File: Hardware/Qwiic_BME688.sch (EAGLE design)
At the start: 30 parts, among them J2 QWIIC_RA, J4 QWIIC_RA, U1 BME688LGA

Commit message: Fixed formatting of examples
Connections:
- net SCL renamed SCL/SCK
- net SDA/POCI renamed SDA/PICO
- removed net SDO: ADR.2, J3.6
- removed net SDO/PICO: U1.SDO
- new net SDO/POCI: ADR.2, J3.6, U1.SDO
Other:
- note added: "NOTE: This circuitry defaults to I2C communication (address 0x76). If you wish to communicate over SPI, please cut the CSB jumper AND the ADR jumper. Remove the I2C pullup resistors by cutting the I2C jumper. Then use the SDO, SDI, SCK, and CSB holes on the board edge."
- note added: "v10"
- note removed: "NOTE: This circuitry defaults to I2C communication (address 0x76). If you wish to communicate over SPI, please cut the CSB jumper AND the ADR jumper. Then use the SDO, SDI, SCK, and CSB holes on the board edge."
- note removed: "v01"
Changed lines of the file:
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@@
 <sheet>
 <plain>
-<text x="237.744" y="7.366" size="2.54" layer="94" font="vector">v01</text>
+<text x="237.744" y="7.366" size="2.54" layer="94" font="vector">v10</text>
 <text x="210.82" y="111.76" size="1.778" layer="97" font="vector" align="center">Default, 7-bit unshifted
 I2C address: 0x76</text>
@@
 0x76). If you wish to communicate
 over SPI, please cut the CSB jumper
-AND the ADR jumper. Then use the
-SDO, SDI, SCK, and CSB holes on the
-board edge.</text>
+AND the ADR jumper. Remove the I2C
+pullup resistors by cutting the I2C
+jumper. Then use the SDO, SDI, SCK,
+and CSB holes on the board edge.</text>
 </plain>
 <instances>
@@
 </segment>
 </net>
-<net name="SCL" class="0">
+<net name="SCL/SCK" class="0">
 <segment>
 <pinref part="J2" gate="G$1" pin="4"/>
@@
 </segment>
 </net>
-<net name="SDA/POCI" class="0">
+<net name="SDA/PICO" class="0">
 <segment>
 <pinref part="J2" gate="G$1" pin="3"/>
@@
 <wire x1="190.5" y1="162.56" x2="193.04" y2="162.56" width="0.1524" layer="91"/>
 <wire x1="193.04" y1="162.56" x2="193.04" y2="160.02" width="0.1524" layer="91"/>
-</segment>
-</net>
-<net name="SDO" class="0">
-<segment>
-<pinref part="ADR" gate="G$1" pin="2"/>
-<wire x1="180.34" y1="93.98" x2="177.8" y2="93.98" width="0.1524" layer="91"/>
-<label x="177.8" y="93.98" size="1.27" layer="95" rot="R180" xref="yes"/>
-</segment>
-<segment>
-<pinref part="J3" gate="G$1" pin="6"/>
-<wire x1="78.74" y1="15.24" x2="73.66" y2="15.24" width="0.1524" layer="91"/>
-<label x="73.66" y="15.24" size="1.27" layer="95" rot="R180" xref="yes"/>
 </segment>
 </net>
@@
 </segment>
 </net>
-<net name="SDO/PICO" class="0">
+<net name="SDO/POCI" class="0">
 <segment>
 <pinref part="U1" gate="U1" pin="SDO"/>
@@
 <label x="142.24" y="93.98" size="1.27" layer="95" xref="yes"/>
 </segment>
-</net>
+<segment>
+<pinref part="ADR" gate="G$1" pin="2"/>
+<wire x1="180.34" y1="93.98" x2="177.8" y2="93.98" width="0.1524" layer="91"/>
+<label x="177.8" y="93.98" size="1.27" layer="95" rot="R180" xref="yes"/>
+</segment>
+<segment>
+<pinref part="J3" gate="G$1" pin="6"/>
+<wire x1="78.74" y1="15.24" x2="73.66" y2="15.24" width="0.1524" layer="91"/>
+<label x="73.66" y="15.24" size="1.27" layer="95" rot="R180" xref="yes"/>
+</segment>
+</net>

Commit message: Updates to hardware v02
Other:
- note added: "v02"
- note removed: "v10"
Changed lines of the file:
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@@
 <sheet>
 <plain>
-<text x="237.744" y="7.366" size="2.54" layer="94" font="vector">v10</text>
+<text x="237.744" y="7.366" size="2.54" layer="94" font="vector">v02</text>
 <text x="210.82" y="111.76" size="1.778" layer="97" font="vector" align="center">Default, 7-bit unshifted
 I2C address: 0x76</text>
@@
 <text x="58.42" y="165.1" size="1.778" layer="97" font="vector">Cut the LED jumper to
 disable the PWR LED</text>
-<text x="187.96" y="165.1" size="1.27" layer="97" font="vector">Cut I2C Jumper to remove
+<text x="187.96" y="165.1" size="1.778" layer="97" font="vector">Cut I2C Jumper to remove
 pullup resistors from the I2C bus</text>
 <text x="12.7" y="177.8" size="2.54" layer="94" font="vector" align="center">LED</text>

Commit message: Update version number
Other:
- note added: "v10"
- note removed: "v02"
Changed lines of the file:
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@@
 <sheet>
 <plain>
-<text x="237.744" y="7.366" size="2.54" layer="94" font="vector">v02</text>
+<text x="237.744" y="7.366" size="2.54" layer="94" font="vector">v10</text>
 <text x="210.82" y="111.76" size="1.778" layer="97" font="vector" align="center">Default, 7-bit unshifted
 I2C address: 0x76</text>

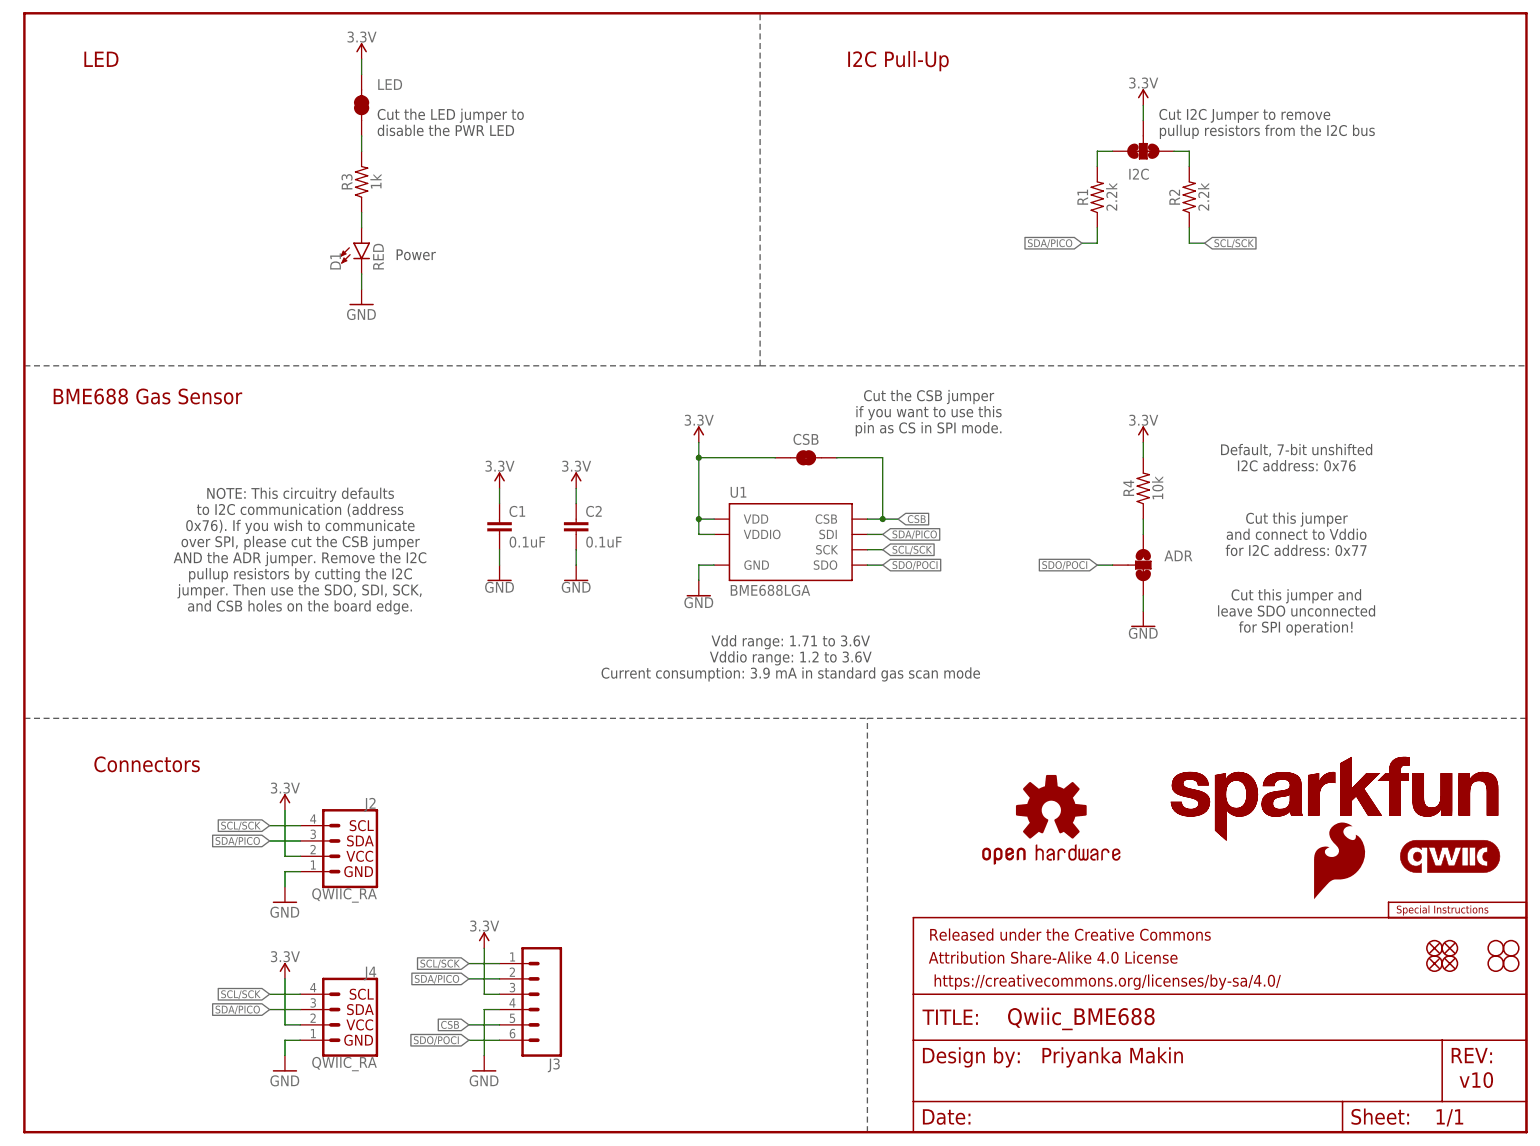
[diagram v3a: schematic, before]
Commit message: Design review changes
* Add table for jumper selection
* Nudge board name silk (on bottom) to avoid vias
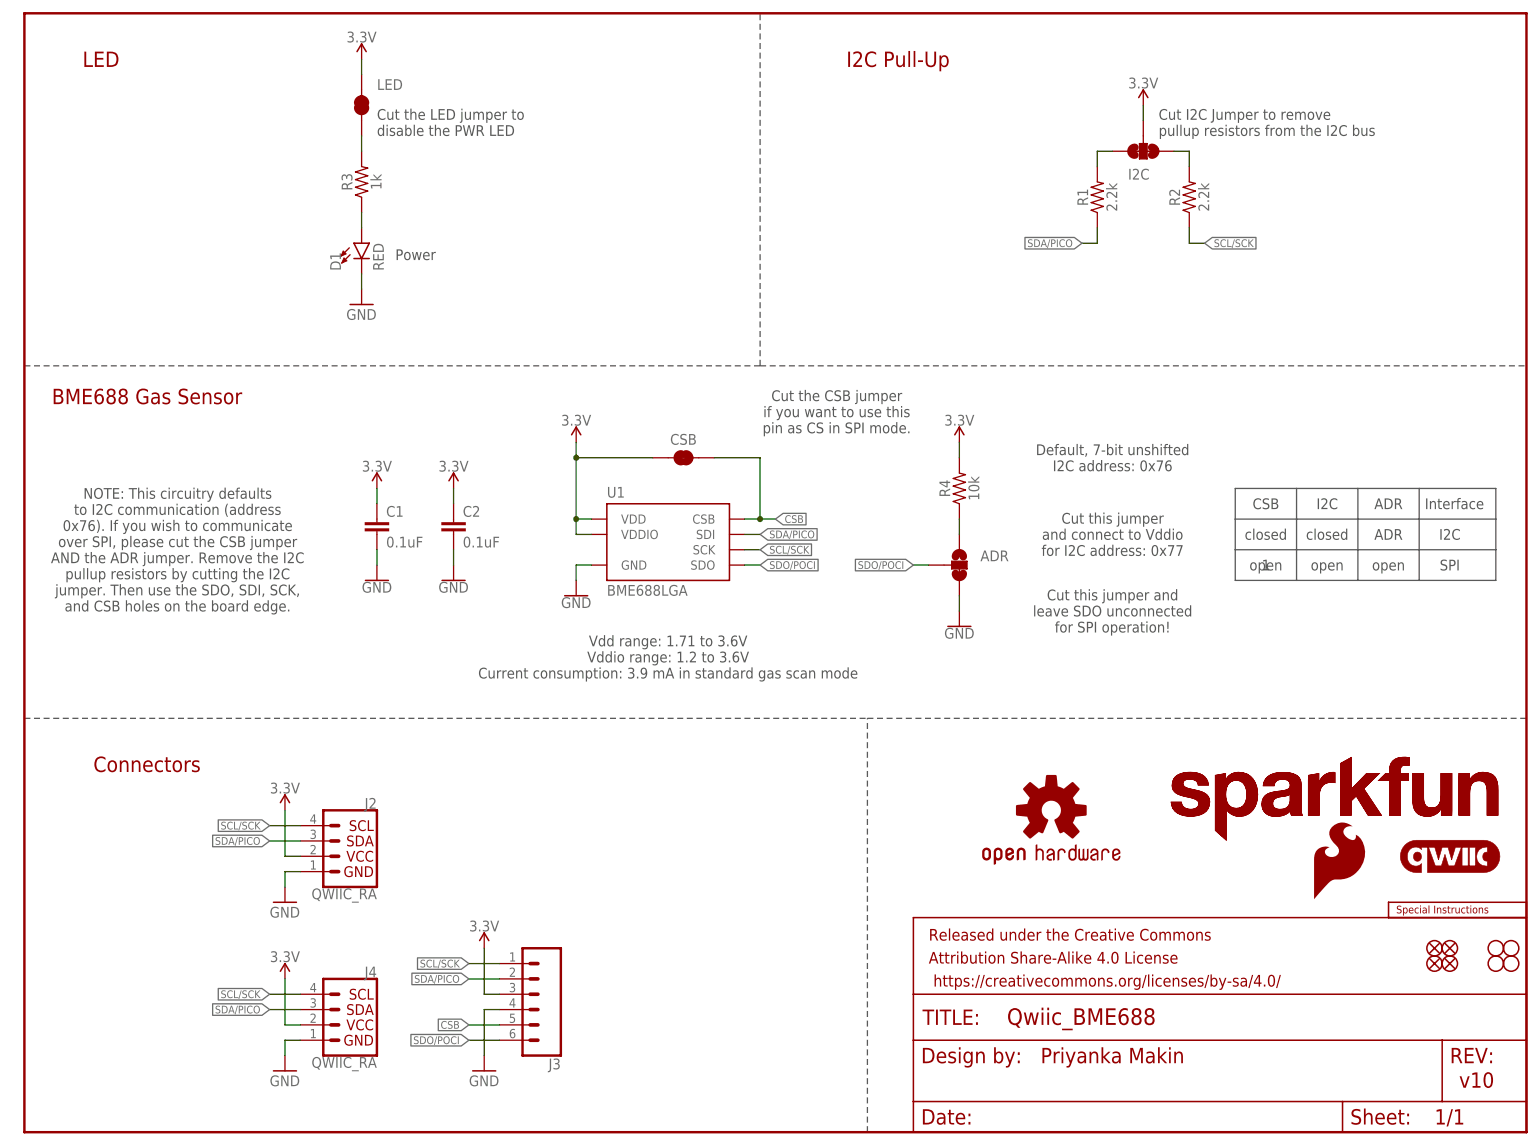
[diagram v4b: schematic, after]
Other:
- note added: "1"
- note added: "ADR"
- note added: "CSB"
- note added: "I2C"
- note added: "Interface"
- note added: "SPI"
- note added: "closed"
- note added: "open"
- moved on the sheet: ADR, C1, C2, CSB, R4, U1

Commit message: QC Double-check:
* Add active low line to "CSB" net label in the schematic
* Updated jumper selection table
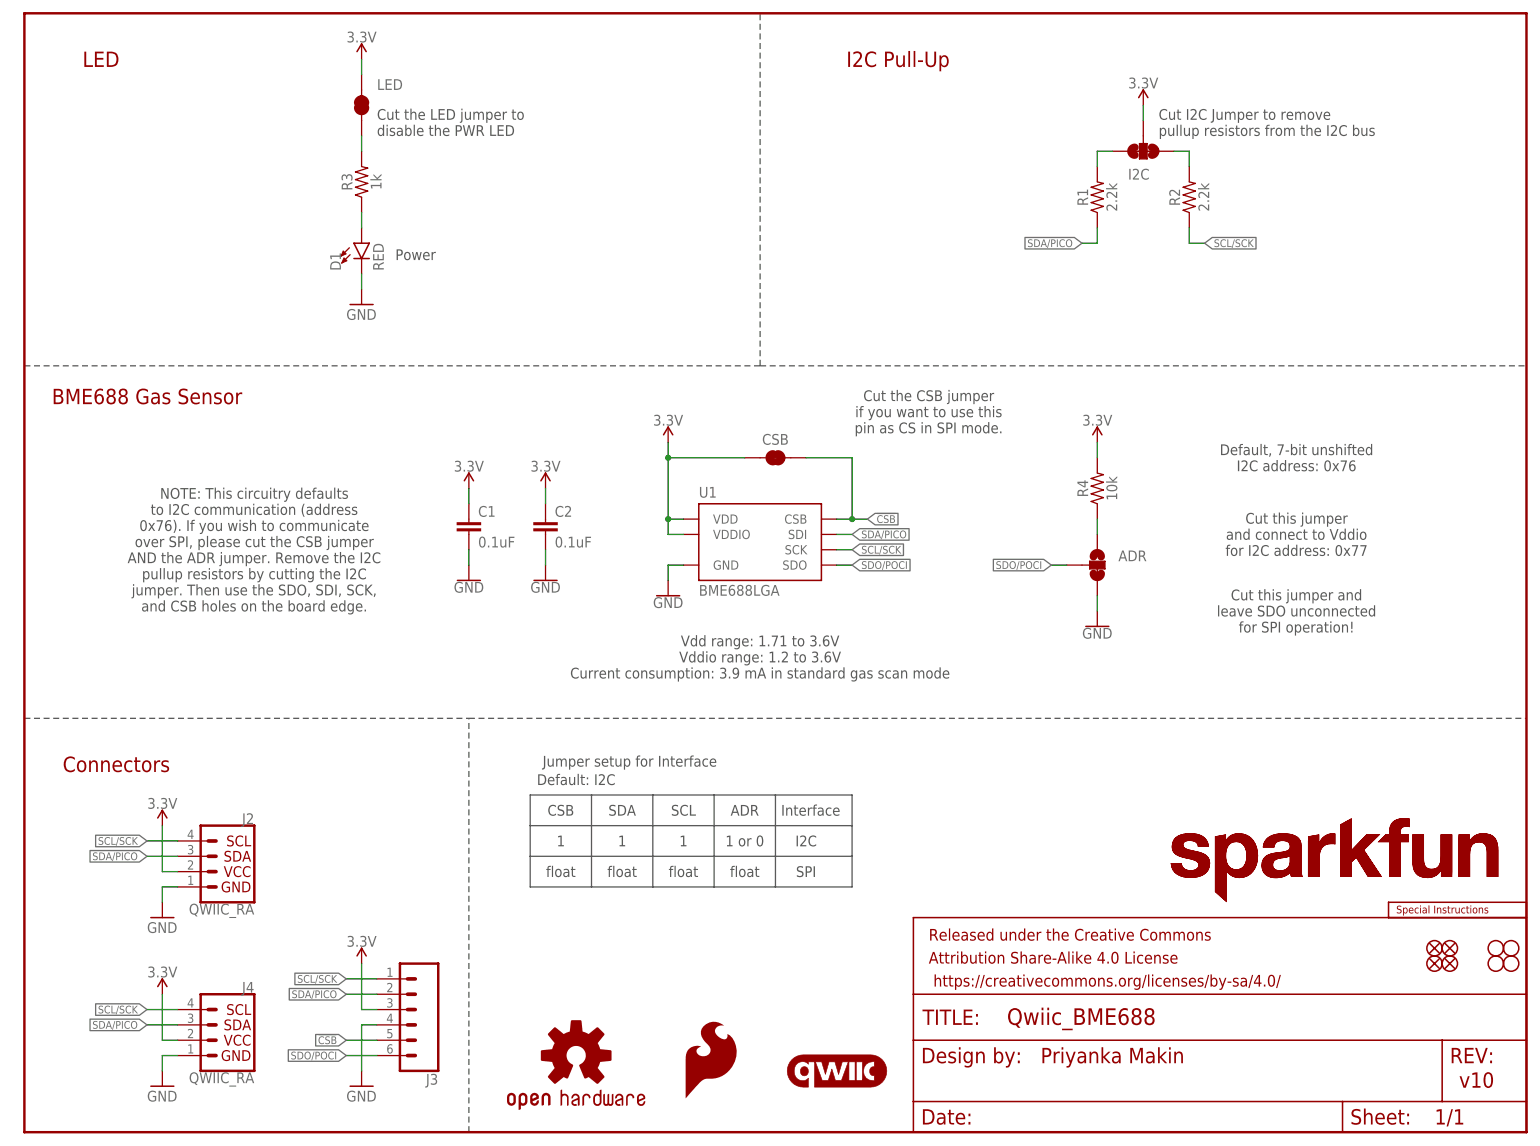
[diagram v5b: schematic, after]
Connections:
- net CSB renamed !CSB!
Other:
- note added: "1 or 0"
- note added: "Default: I2C"
- note added: "Jumper setup for Interface"
- note added: "SCL"
- note added: "SDA"
- note added: "float"
- note removed: "closed"
- note removed: "open"
- moved on the sheet: ADR, C1, C2, CSB, J2, J3, J4, R4, U1

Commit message: Update BME688 schematic symbol
* CSB pin to !CSB!
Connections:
- net !CSB!: now also U1.!CSB!; no longer U1.CSB
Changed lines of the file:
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@@
 <net name="!CSB!" class="0">
 <segment>
-<pinref part="U1" gate="U1" pin="CSB"/>
+<pinref part="U1" gate="U1" pin="!CSB!"/>
 <wire x1="134.62" y1="101.6" x2="137.16" y2="101.6" width="0.1524" layer="91"/>
 <label x="139.7" y="101.6" size="1.27" layer="95" xref="yes"/>
@@
 </sheet>
 </sheets>
-<errors>
-</errors>
 </schematic>
 </drawing>

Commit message: Rename PICO/POCI net labels to CIPO/COPI
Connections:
- net SDA/PICO renamed SDA/COPI
- net SDO/POCI renamed SDO/CIPO
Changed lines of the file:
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@@
 </segment>
 </net>
-<net name="SDA/PICO" class="0">
+<net name="SDA/COPI" class="0">
 <segment>
 <pinref part="J2" gate="G$1" pin="3"/>
@@
 </segment>
 </net>
-<net name="SDO/POCI" class="0">
+<net name="SDO/CIPO" class="0">
 <segment>
 <pinref part="U1" gate="U1" pin="SDO"/>

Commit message: Rename PICO/POCI labels to SDO/SDI
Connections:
- net SDA/COPI renamed SDI/SDA
- net SDO/CIPO renamed SDO
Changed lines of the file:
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@@
 </segment>
 </net>
-<net name="SDA/COPI" class="0">
+<net name="SDI/SDA" class="0">
 <segment>
 <pinref part="J2" gate="G$1" pin="3"/>
@@
 </segment>
 </net>
-<net name="SDO/CIPO" class="0">
+<net name="SDO" class="0">
 <segment>
 <pinref part="U1" gate="U1" pin="SDO"/>
